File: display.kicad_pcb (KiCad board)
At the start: 2 copper layers, 165.1 x 57.1 mm, 122 parts, among them P1 CONN_02X14, P2 CONN_02X15, Q1 BC846, Q10 BC846, Q11 BC856, Q12 BC856, Q13 BC846, Q14 BC846, Q15 BC856, Q16 BC856, Q17 BC846, Q18 BC846, Q19 BC856, Q2 BC846, Q20 BC856, Q21 BC846, Q22 BC846, Q23 BC856, Q24 BC856, Q25 BC846, Q26 BC846, Q27 BC856, Q28 BC856, Q29 BC846, Q3 BC856, Q30 BC846, Q31 BC856, Q32 BC856, Q33 BC846, Q34 BC846, Q35 BC856, Q36 BC856, Q37 BC846, Q38 BC846, Q39 BC856, Q4 BC856, Q40 BC856, Q41 BC846, Q42 BC846, Q43 BC856, Q44 BC856, Q45 BC846, Q46 BC846, Q47 BC856, Q48 BC856, Q5 BC846, Q6 BC846, Q7 BC856, Q8 BC856, Q9 BC846

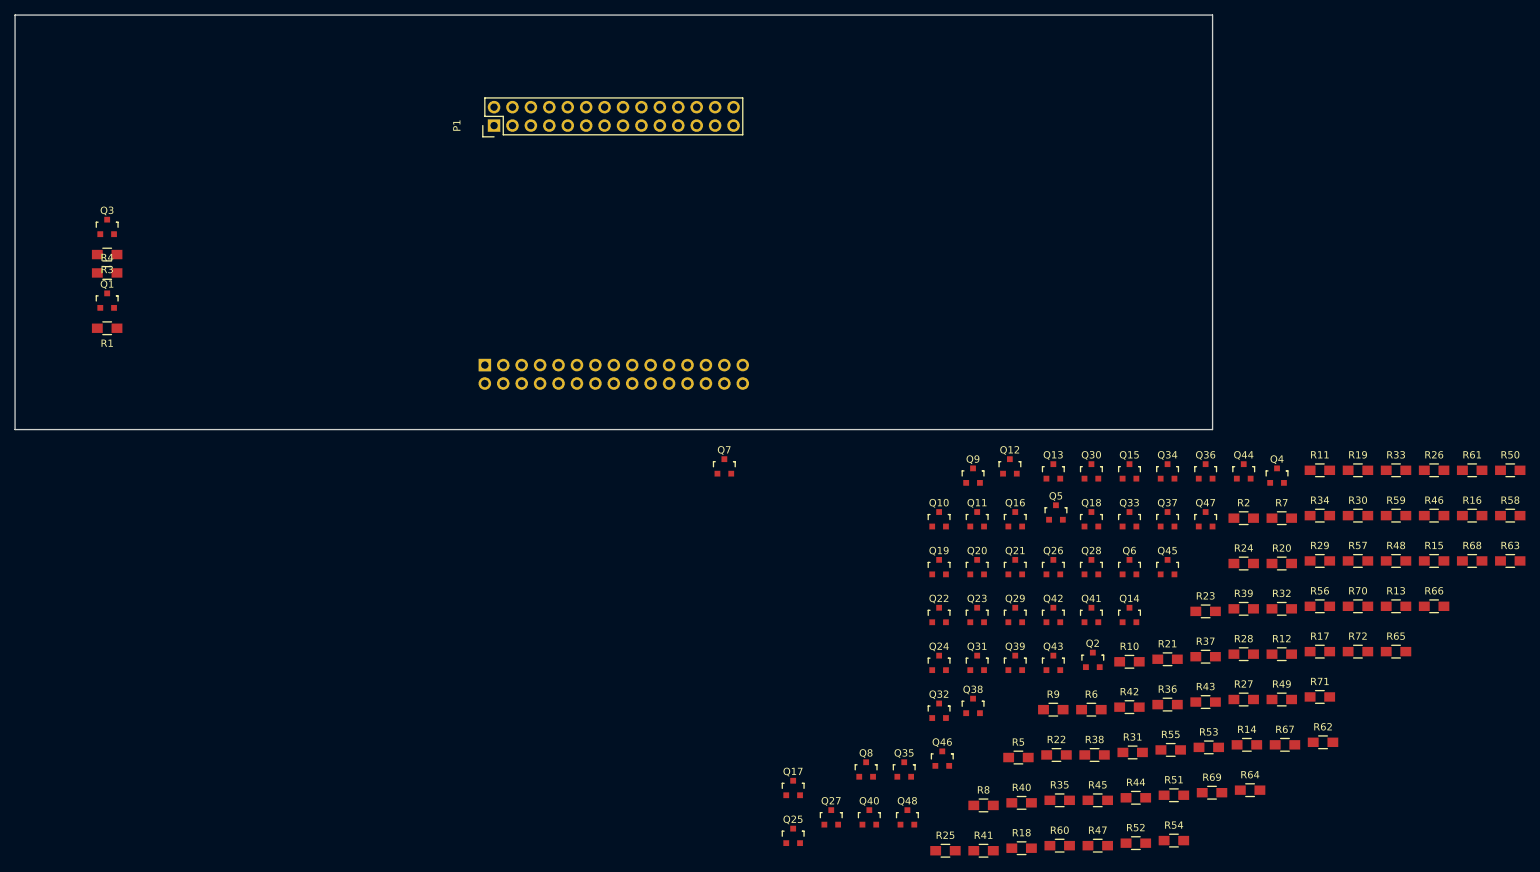
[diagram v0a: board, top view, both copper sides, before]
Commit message: Placement finalizing and some small routing.
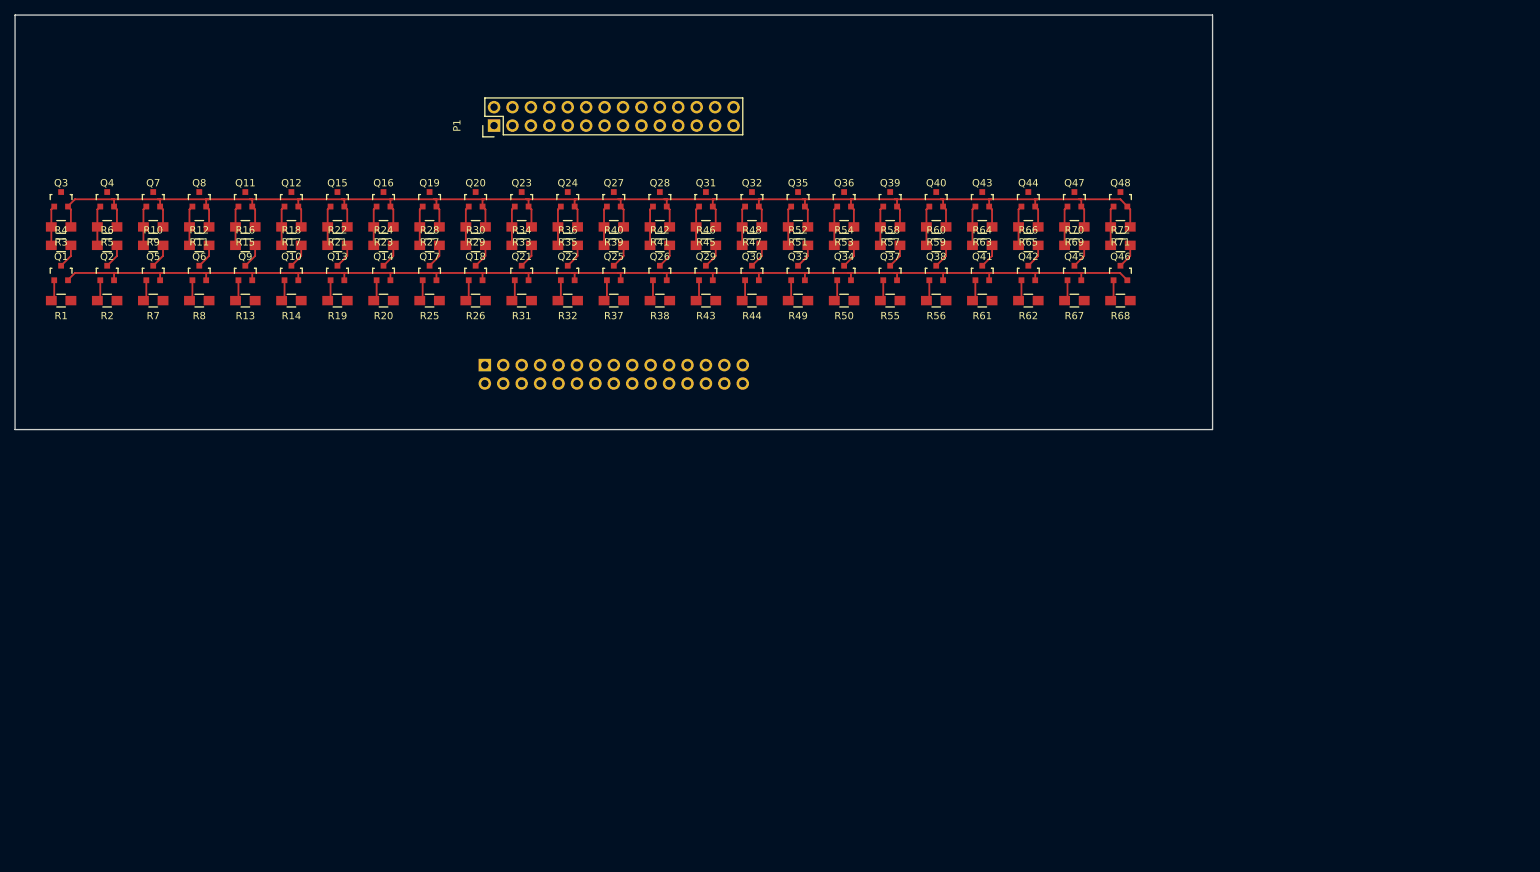
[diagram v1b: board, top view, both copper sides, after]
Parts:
- moved R16 173.2 mm to (95.2, 85.1)
- moved R15 170.2 mm to (95.2, 82.5), turned to 180 degrees
- moved Q4 165.7 mm to (76.2, 78.7)
- moved R13 164.1 mm to (95.2, 92.7), turned to 180 degrees
- moved R2 159.5 mm to (76.2, 92.7), turned to 180 degrees
- moved R12 159.5 mm to (88.9, 85.1)
- moved R7 158.5 mm to (82.5, 92.7), turned to 180 degrees
- moved R11 158.1 mm to (88.9, 82.5), turned to 180 degrees
- moved R17 153.4 mm to (101.6, 82.5), turned to 180 degrees
- moved R6 150.0 mm to (76.2, 85.1)
- moved R10 146.3 mm to (82.5, 85.1)
- moved Q2 146.0 mm to (76.2, 88.9)
- moved R5 145.4 mm to (76.2, 82.5), turned to 180 degrees
- moved R14 145.3 mm to (101.6, 92.7), turned to 180 degrees
- moved R19 142.6 mm to (108.0, 92.7), turned to 180 degrees
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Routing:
- net /+40V: track 0.00 -> 247.3 mm
- net /GND: track 0.00 -> 175.9 mm
- net Net-(Q8-Pad1): track 0.00 -> 5.51 mm
- net Net-(Q47-Pad1): track 0.00 -> 5.51 mm
- net Net-(Q44-Pad1): track 0.00 -> 5.51 mm
- net Net-(Q43-Pad1): track 0.00 -> 5.51 mm
- net Net-(Q40-Pad1): track 0.00 -> 5.51 mm
- net Net-(Q4-Pad1): track 0.00 -> 5.51 mm
- net Net-(Q36-Pad1): track 0.00 -> 5.51 mm
- net Net-(Q35-Pad1): track 0.00 -> 5.51 mm
- net Net-(Q32-Pad1): track 0.00 -> 5.51 mm
- net Net-(Q31-Pad1): track 0.00 -> 5.51 mm
- net Net-(Q3-Pad1): track 0.00 -> 5.51 mm
- net Net-(Q27-Pad1): track 0.00 -> 5.51 mm
- net Net-(Q24-Pad1): track 0.00 -> 5.51 mm
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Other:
- net class Default: clearance 0.2 -> 0.254; trace_width 0.25 -> 0.254; via_dia 0.6 -> 0.6858; via_drill 0.4 -> 0.3302
- net class Kathode added: clearance 0.254, trace_width 0.762, via_dia 0.6858, via_drill 0.3302
- rule trace_clearance: 0.2 -> 0.254
- rule trace_min: 0.2 -> 0.254
- rule via_min_drill: 0.3 -> 0.3302
- rule via_min_size: 0.4 -> 0.6858

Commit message: Finishing layout, generating gerbers.
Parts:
- Q1, Q10, Q11, Q12, Q13, Q14, Q15, Q16, Q17, Q18, Q19, Q2, Q20, Q21, Q22, Q23, Q24, Q25, Q26, Q27, Q28, Q29, Q3, Q30, Q31, Q32, Q33, Q34, Q35, Q36, Q37, Q38, Q39, Q4, Q40, Q41, Q42, Q43, Q44, Q45, Q46, Q47, Q48, Q5, Q6, Q7, Q8, Q9: footprint TO_SOT_Packages_SMD:SOT-23 -> TO_SOT_Packages_SMD:SOT-23_Handsoldering
- moved P1 3.81 mm to (129.5, 64.8)
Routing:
- net /K1: track 0.00 -> 71.4 mm
- net Net-(P1-Pad3): track 0.00 -> 70.2 mm
- net Net-(P1-Pad4): track 0.00 -> 68.6 mm
- net Net-(P1-Pad26): track 0.00 -> 66.1 mm
- net Net-(P2-Pad26): track 0.00 -> 64.4 mm
- net Net-(P2-Pad3): track 0.00 -> 63.7 mm
- net Net-(P2-Pad4): track 0.00 -> 62.0 mm
- net Net-(P1-Pad5): track 0.00 -> 60.8 mm
- net Net-(P1-Pad6): track 0.00 -> 58.8 mm
- net Net-(P1-Pad25): track 0.00 -> 58.3 mm
- net Net-(P1-Pad24): track 0.00 -> 56.6 mm
- net Net-(P2-Pad25): track 0.00 -> 56.6 mm
- net Net-(P2-Pad24): track 0.00 -> 54.9 mm
- net Net-(P2-Pad5): track 0.00 -> 54.2 mm
- net Net-(P2-Pad6): track 0.00 -> 52.6 mm
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- added copper zone on B.Cu, net /GND
